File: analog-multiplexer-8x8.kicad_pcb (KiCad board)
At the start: 2 copper layers, 70.4 x 165.1 mm, 30 parts, among them J1 Conn_01x13, J2 Conn_02x08_Odd_Even, U1 4051, U2 4051, U3 4051, U4 4051, U5 4051, U6 4051, U7 4051, U8 4051

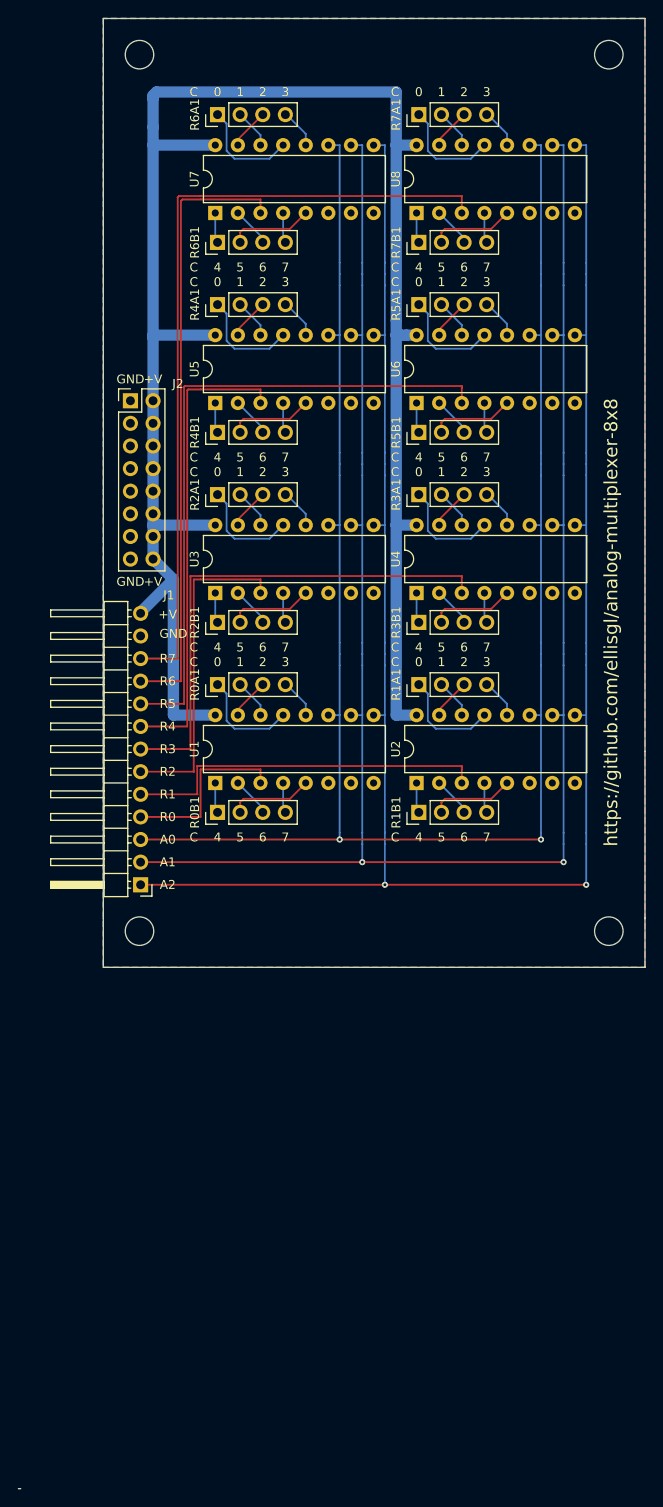
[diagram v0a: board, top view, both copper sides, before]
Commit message: Changed 8mil tracks to 10mil.
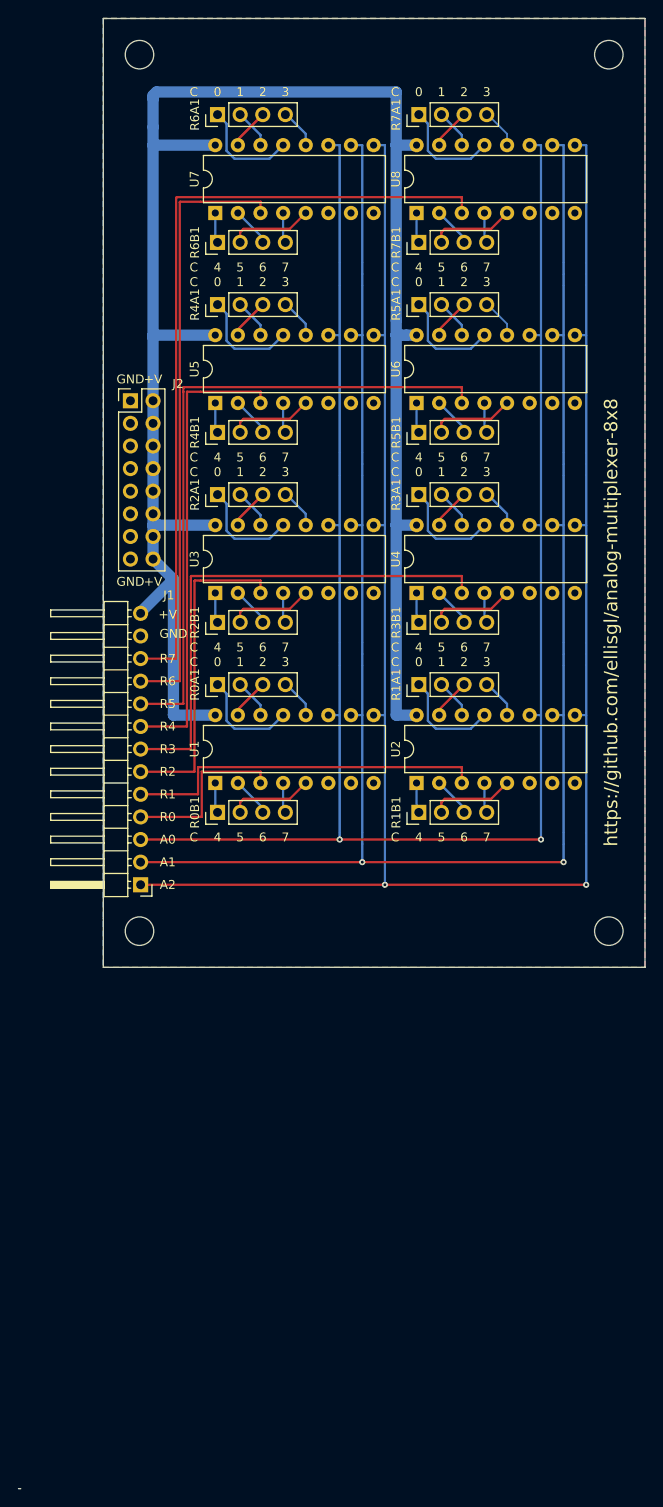
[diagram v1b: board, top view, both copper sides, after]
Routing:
- net A2: track 226.3 -> 393.7 mm
- net A1: track 218.7 -> 381.0 mm
- net A0: track 211.1 -> 368.3 mm
- net Net-(R6A1-Pad1): track 11.8 -> 21.5 mm
- net Net-(R2A1-Pad1): track 11.8 -> 21.5 mm
- net Net-(R0A1-Pad1): track 11.8 -> 21.5 mm
- net Net-(R3A1-Pad1): track 11.8 -> 21.5 mm
- net Net-(R7A1-Pad1): track 11.8 -> 21.5 mm
- net Net-(R1A1-Pad1): track 11.8 -> 21.5 mm
- net Net-(R5A1-Pad1): track 11.8 -> 21.5 mm
- net Net-(R4A1-Pad1): track 11.8 -> 21.5 mm
- net Net-(R7B1-Pad2): track 9.40 -> 16.3 mm
- net Net-(R4B1-Pad2): track 9.40 -> 16.3 mm
- net Net-(R2B1-Pad2): track 9.40 -> 16.3 mm
- net Net-(R0B1-Pad2): track 9.40 -> 16.3 mm
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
